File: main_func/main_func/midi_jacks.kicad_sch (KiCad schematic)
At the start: 13 parts, among them J4 MIDI_IN, J5 MIDI_THRU, J6 MIDI_OUT, J7 AudioJack4_Ground_SwitchTR1, J8 Conn_01x02_Male, U5 6N137

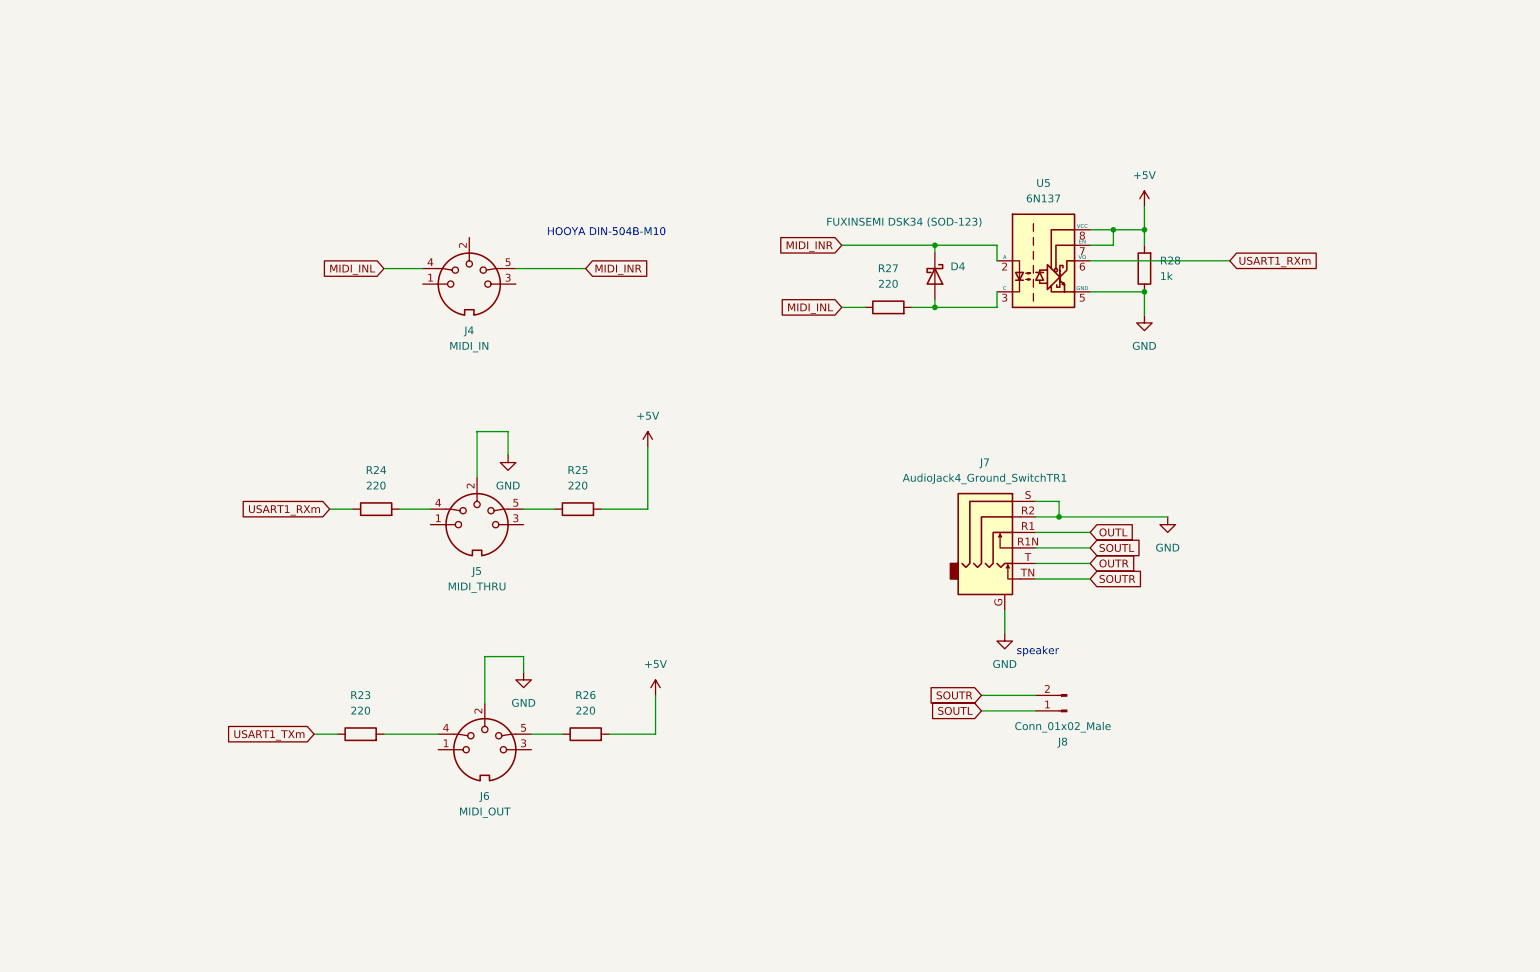
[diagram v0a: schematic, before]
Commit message: main func schematics fixed
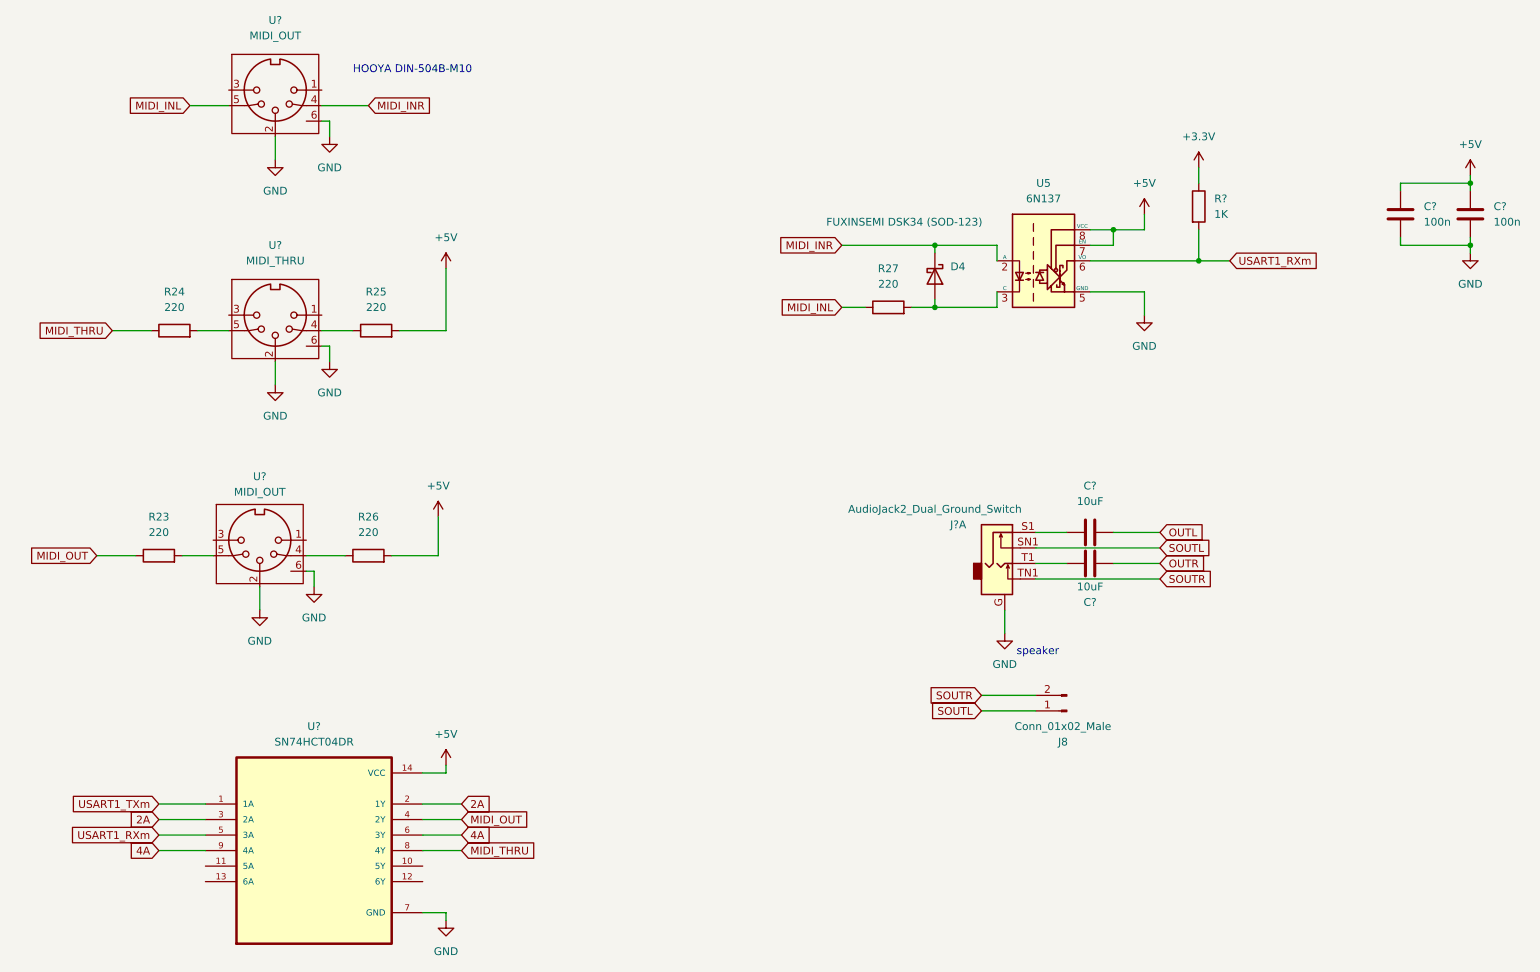
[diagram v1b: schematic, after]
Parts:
- removed J4: MIDI_IN, symbol Connector:DIN-5_180degree
- removed J5: MIDI_THRU, symbol Connector:DIN-5_180degree
- removed J6: MIDI_OUT, symbol Connector:DIN-5_180degree
- removed J7: AudioJack4_Ground_SwitchTR1, symbol Connector:AudioJack4_Ground_SwitchTR1
- removed R28: 1k, Resistor_SMD:R_0805_2012Metric_Pad1.20x1.40mm_HandSolder, symbol Device:R
- added C? (x2): 100n, Capacitor_SMD:C_0805_2012Metric_Pad1.18x1.45mm_HandSolder, symbol Device:C
- added C? (x2): 10uF, Capacitor_SMD:C_0805_2012Metric_Pad1.18x1.45mm_HandSolder, symbol Device:C
- added J?: AudioJack2_Dual_Ground_Switch, symbol Connector:AudioJack2_Dual_Ground_Switch
- added R?: 1K, Resistor_SMD:R_0805_2012Metric_Pad1.20x1.40mm_HandSolder, symbol Device:R
- added U? (x2): MIDI_OUT, midi:midi_7pin, symbol midi:midi5(+2)
- added U?: SN74HCT04DR, Package_SO:SOIC-14_3.9x8.7mm_P1.27mm, symbol SN74HCT04N:SN74HCT04N
- added U?: MIDI_THRU, midi:midi_7pin, symbol midi:midi5(+2)
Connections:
- net +5V: now also C?.1, C?.1, U?.14 (VCC)
- net GND: now also C?.2, C?.2, J?.G, U?.2, U?.2, U?.2, U?.6, U?.6, U?.6, U?.7 (GND)
- net MIDI_INL: now also U?.5
- net MIDI_INR: now also U?.4
- net OUTL: now also C?.2
- net OUTR: now also C?.2
- net SOUTL: now also J?.SN1
- net SOUTR: now also J?.TN1
- net USART1_RXm: now also R?.2, U?.5 (3A); no longer R24.1
- net USART1_TXm: now also U?.1 (1A); no longer R23.1
- net at R23.2: now also U?.5
- net at R24.2: now also U?.5
- net at R25.1: now also U?.4
- net at R26.1: now also U?.4
- new net: C?.1, J?.S1
- new net: C?.1, J?.T1
- new net +3V3: R?.1
- new net 2A: U?.2 (1Y), U?.3 (2A)
- new net 4A: U?.6 (3Y), U?.9 (4A)
- new net MIDI_OUT: R23.1, U?.4 (2Y)
- new net MIDI_THRU: R24.1, U?.8 (4Y)
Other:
- moved on the sheet: R23, R24, R25, R26

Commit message: fixing keyboard and pot project schematics
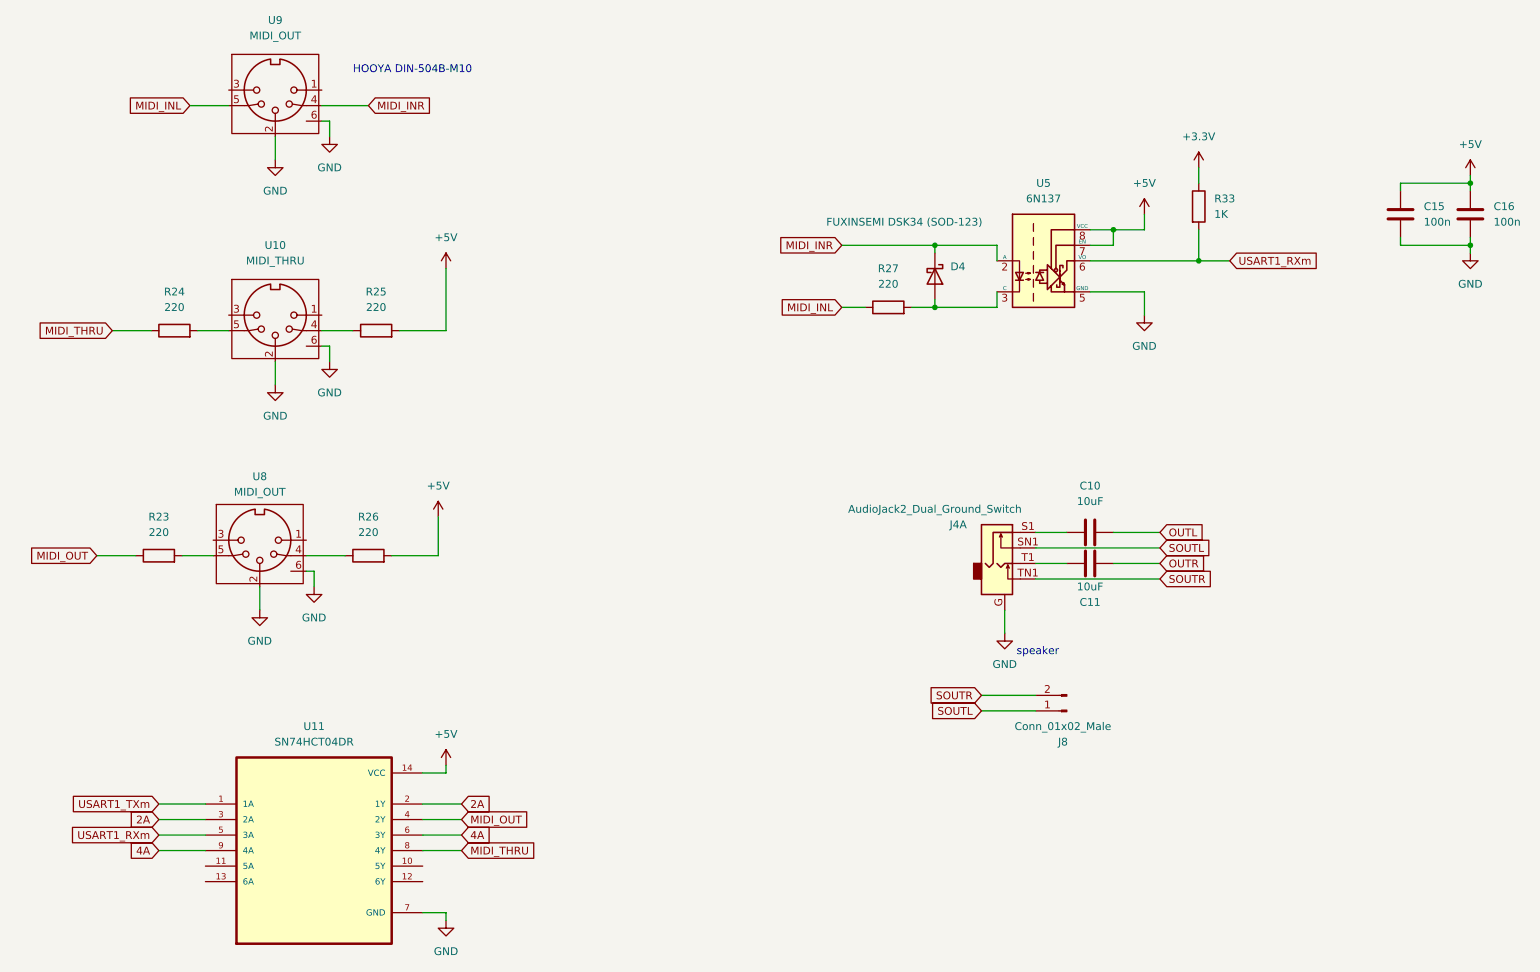
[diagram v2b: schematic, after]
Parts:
- gave numbers to parts that had none: 10
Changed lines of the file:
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@@
   (symbol (lib_id "midi:midi5(+2)") (at 63.5 32.766 0) (unit 1)
     (in_bom yes) (on_board yes) (fields_autoplaced)
-    (property "Reference" "U?" (id 0) (at 63.5 13.97 0))
+    (property "Reference" "U9" (id 0) (at 63.5 13.97 0))
     (property "Value" "MIDI_OUT" (id 1) (at 63.5 16.51 0))
     (property "Footprint" "midi:midi_7pin" (id 2) (at 86.868 23.876 0)
@@
   (symbol (lib_id "SN74HCT04N:SN74HCT04N") (at 69.85 149.86 0) (unit 1)
     (in_bom yes) (on_board yes) (fields_autoplaced)
-    (property "Reference" "U?" (id 0) (at 69.85 129.54 0))
+    (property "Reference" "U11" (id 0) (at 69.85 129.54 0))
     (property "Value" "SN74HCT04DR" (id 1) (at 69.85 132.08 0))
     (property "Footprint" "Package_SO:SOIC-14_3.9x8.7mm_P1.27mm" (id 2) (at 69.85 149.86 0)
@@
   (symbol (lib_id "power:GND") (at 63.5 36.83 0) (unit 1)
     (in_bom yes) (on_board yes) (fields_autoplaced)
-    (property "Reference" "#PWR?" (id 0) (at 63.5 43.18 0)
+    (property "Reference" "#PWR013" (id 0) (at 63.5 43.18 0)
       (effects (font (size 1.27 1.27)) hide)
     )
@@
   (symbol (lib_id "power:GND") (at 72.39 33.02 0) (unit 1)
     (in_bom yes) (on_board yes) (fields_autoplaced)
-    (property "Reference" "#PWR?" (id 0) (at 72.39 39.37 0)
+    (property "Reference" "#PWR015" (id 0) (at 72.39 39.37 0)
       (effects (font (size 1.27 1.27)) hide)
     )
@@
   (symbol (lib_id "power:+5V") (at 259.08 39.37 0) (unit 1)
     (in_bom yes) (on_board yes) (fields_autoplaced)
-    (property "Reference" "#PWR?" (id 0) (at 259.08 43.18 0)
+    (property "Reference" "#PWR023" (id 0) (at 259.08 43.18 0)
       (effects (font (size 1.27 1.27)) hide)
     )
@@
   (symbol (lib_id "power:GND") (at 91.44 161.29 0) (unit 1)
     (in_bom yes) (on_board yes) (fields_autoplaced)
-    (property "Reference" "#PWR?" (id 0) (at 91.44 167.64 0)
+    (property "Reference" "#PWR020" (id 0) (at 91.44 167.64 0)
       (effects (font (size 1.27 1.27)) hide)
     )
@@
   (symbol (lib_id "Connector:AudioJack2_Dual_Ground_Switch") (at 182.88 102.87 0) (unit 1)
     (in_bom yes) (on_board yes)
-    (property "Reference" "J?" (id 0) (at 175.26 96.52 0))
+    (property "Reference" "J4" (id 0) (at 175.26 96.52 0))
     (property "Value" "AudioJack2_Dual_Ground_Switch" (id 1) (at 171.45 93.98 0))
     (property "Footprint" "" (id 2) (at 181.61 97.79 0)
@@
   (symbol (lib_id "power:GND") (at 259.08 52.07 0) (unit 1)
     (in_bom yes) (on_board yes) (fields_autoplaced)
-    (property "Reference" "#PWR?" (id 0) (at 259.08 58.42 0)
+    (property "Reference" "#PWR025" (id 0) (at 259.08 58.42 0)
       (effects (font (size 1.27 1.27)) hide)
     )
@@
   (symbol (lib_id "Device:R") (at 214.63 44.45 0) (unit 1)
     (in_bom yes) (on_board yes) (fields_autoplaced)
-    (property "Reference" "R?" (id 0) (at 217.17 43.1799 0)
+    (property "Reference" "R33" (id 0) (at 217.17 43.1799 0)
       (effects (font (size 1.27 1.27)) (justify left))
     )
@@
   (symbol (lib_id "power:GND") (at 69.85 106.68 0) (unit 1)
     (in_bom yes) (on_board yes) (fields_autoplaced)
-    (property "Reference" "#PWR?" (id 0) (at 69.85 113.03 0)
+    (property "Reference" "#PWR014" (id 0) (at 69.85 113.03 0)
       (effects (font (size 1.27 1.27)) hide)
     )
@@
   (symbol (lib_id "midi:midi5(+2)") (at 63.5 69.596 0) (unit 1)
     (in_bom yes) (on_board yes) (fields_autoplaced)
-    (property "Reference" "U?" (id 0) (at 63.5 50.8 0))
+    (property "Reference" "U10" (id 0) (at 63.5 50.8 0))
     (property "Value" "MIDI_THRU" (id 1) (at 63.5 53.34 0))
     (property "Footprint" "midi:midi_7pin" (id 2) (at 86.868 60.706 0)
@@
   (symbol (lib_id "power:+3.3V") (at 214.63 38.1 0) (unit 1)
     (in_bom yes) (on_board yes) (fields_autoplaced)
-    (property "Reference" "#PWR?" (id 0) (at 214.63 41.91 0)
+    (property "Reference" "#PWR021" (id 0) (at 214.63 41.91 0)
       (effects (font (size 1.27 1.27)) hide)
     )
@@
   (symbol (lib_id "Device:C") (at 247.65 45.72 0) (unit 1)
     (in_bom yes) (on_board yes) (fields_autoplaced)
-    (property "Reference" "C?" (id 0) (at 251.46 44.4499 0)
+    (property "Reference" "C15" (id 0) (at 251.46 44.4499 0)
       (effects (font (size 1.27 1.27)) (justify left))
     )
@@
   (symbol (lib_id "Device:C") (at 196.85 97.79 90) (unit 1)
     (in_bom yes) (on_board yes) (fields_autoplaced)
-    (property "Reference" "C?" (id 0) (at 196.85 90.17 90))
+    (property "Reference" "C10" (id 0) (at 196.85 90.17 90))
     (property "Value" "10uF" (id 1) (at 196.85 92.71 90))
     (property "Footprint" "Capacitor_SMD:C_0805_2012Metric_Pad1.18x1.45mm_HandSolder" (id 2) (at 200.66 96.8248 0)
@@
   (symbol (lib_id "power:GND") (at 72.39 69.85 0) (unit 1)
     (in_bom yes) (on_board yes) (fields_autoplaced)
-    (property "Reference" "#PWR?" (id 0) (at 72.39 76.2 0)
+    (property "Reference" "#PWR018" (id 0) (at 72.39 76.2 0)
       (effects (font (size 1.27 1.27)) hide)
     )
@@
   (symbol (lib_id "power:+5V") (at 91.44 135.89 0) (unit 1)
     (in_bom yes) (on_board yes) (fields_autoplaced)
-    (property "Reference" "#PWR?" (id 0) (at 91.44 139.7 0)
+    (property "Reference" "#PWR019" (id 0) (at 91.44 139.7 0)
       (effects (font (size 1.27 1.27)) hide)
     )
@@
   (symbol (lib_id "Device:C") (at 196.85 102.87 90) (unit 1)
     (in_bom yes) (on_board yes)
-    (property "Reference" "C?" (id 0) (at 196.85 109.22 90))
+    (property "Reference" "C11" (id 0) (at 196.85 109.22 90))
     (property "Value" "10uF" (id 1) (at 196.85 106.68 90))
     (property "Footprint" "Capacitor_SMD:C_0805_2012Metric_Pad1.18x1.45mm_HandSolder" (id 2) (at 200.66 101.9048 0)
@@
   (symbol (lib_id "Device:C") (at 259.08 45.72 0) (unit 1)
     (in_bom yes) (on_board yes) (fields_autoplaced)
-    (property "Reference" "C?" (id 0) (at 262.89 44.4499 0)
+    (property "Reference" "C16" (id 0) (at 262.89 44.4499 0)
       (effects (font (size 1.27 1.27)) (justify left))
     )
@@
   (symbol (lib_id "midi:midi5(+2)") (at 60.96 106.426 0) (unit 1)
     (in_bom yes) (on_board yes) (fields_autoplaced)
-    (property "Reference" "U?" (id 0) (at 60.96 88.646 0))
+    (property "Reference" "U8" (id 0) (at 60.96 88.646 0))
     (property "Value" "MIDI_OUT" (id 1) (at 60.96 91.186 0))
     (property "Footprint" "midi:midi_7pin" (id 2) (at 84.328 97.536 0)

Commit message: main_func pcb done
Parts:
- C10, C11: value 10uF -> 10u; footprint Capacitor_SMD:C_0805_2012Metric_Pad1.18x1.45mm_HandSolder -> Capacitor_THT:C_Rect_L33.0mm_W15.0mm_P27.50mm_MKS4
- J4: value AudioJack2_Dual_Ground_Switch -> Korean Hroparts Elec PJ-3250-5A; footprint (none) -> Korean Hroparts Elec PJ-3250-5A:Korean Hroparts Elec PJ-3250-5A
- J8: footprint (none) -> Connector_PinSocket_2.54mm:PinSocket_1x02_P2.54mm_Horizontal
- U9: value MIDI_OUT -> MIDI_IN
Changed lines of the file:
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@@
   (global_label "USART1_RXm" (shape input) (at 44.45 147.32 180) (fields_autoplaced)
     (effects (font (size 1.27 1.27)) (justify right))
-    (property "Intersheet References" "${INTERSHEET_REFS}" (id 0) (at 29.8207 147.3994 0)
+    (property "Intersheet References" "${INTERSHEET_REFS}" (id 0) (at 29.8207 147.2406 0)
       (effects (font (size 1.27 1.27)) (justify right) hide)
     )
@@
   (global_label "USART1_TXm" (shape input) (at 44.45 142.24 180) (fields_autoplaced)
     (effects (font (size 1.27 1.27)) (justify right))
-    (property "Intersheet References" "${INTERSHEET_REFS}" (id 0) (at 30.1231 142.3194 0)
+    (property "Intersheet References" "${INTERSHEET_REFS}" (id 0) (at 30.1231 142.1606 0)
       (effects (font (size 1.27 1.27)) (justify right) hide)
     )
@@
     (in_bom yes) (on_board yes) (fields_autoplaced)
     (property "Reference" "U9" (id 0) (at 63.5 13.97 0))
-    (property "Value" "MIDI_OUT" (id 1) (at 63.5 16.51 0))
+    (property "Value" "MIDI_IN" (id 1) (at 63.5 16.51 0))
     (property "Footprint" "midi:midi_7pin" (id 2) (at 86.868 23.876 0)
       (effects (font (size 1.27 1.27)) hide)
@@
     (property "Reference" "J8" (id 0) (at 192.405 132.08 0))
     (property "Value" "Conn_01x02_Male" (id 1) (at 192.405 129.54 0))
-    (property "Footprint" "" (id 2) (at 193.04 127 0)
+    (property "Footprint" "Connector_PinSocket_2.54mm:PinSocket_1x02_P2.54mm_Horizontal" (id 2) (at 193.04 127 0)
       (effects (font (size 1.27 1.27)) hide)
     )
@@
     (in_bom yes) (on_board yes)
     (property "Reference" "J4" (id 0) (at 175.26 96.52 0))
-    (property "Value" "AudioJack2_Dual_Ground_Switch" (id 1) (at 171.45 93.98 0))
-    (property "Footprint" "" (id 2) (at 181.61 97.79 0)
+    (property "Value" "Korean Hroparts Elec PJ-3250-5A" (id 1) (at 171.45 93.98 0))
+    (property "Footprint" "Korean Hroparts Elec PJ-3250-5A:Korean Hroparts Elec PJ-3250-5A" (id 2) (at 181.61 97.79 0)
       (effects (font (size 1.27 1.27)) hide)
     )
@@
     (in_bom yes) (on_board yes) (fields_autoplaced)
     (property "Reference" "C10" (id 0) (at 196.85 90.17 90))
-    (property "Value" "10uF" (id 1) (at 196.85 92.71 90))
-    (property "Footprint" "Capacitor_SMD:C_0805_2012Metric_Pad1.18x1.45mm_HandSolder" (id 2) (at 200.66 96.8248 0)
+    (property "Value" "10u" (id 1) (at 196.85 92.71 90))
+    (property "Footprint" "Capacitor_THT:C_Rect_L33.0mm_W15.0mm_P27.50mm_MKS4" (id 2) (at 200.66 96.8248 0)
       (effects (font (size 1.27 1.27)) hide)
     )
@@
     (in_bom yes) (on_board yes)
     (property "Reference" "C11" (id 0) (at 196.85 109.22 90))
-    (property "Value" "10uF" (id 1) (at 196.85 106.68 90))
-    (property "Footprint" "Capacitor_SMD:C_0805_2012Metric_Pad1.18x1.45mm_HandSolder" (id 2) (at 200.66 101.9048 0)
-      (effects (font (size 1.27 1.27)) hide)
-    )
+    (property "Value" "10u" (id 1) (at 196.85 106.68 90))
+    (property "Footprint" "Capacitor_THT:C_Rect_L33.0mm_W15.0mm_P27.50mm_MKS4" (id 2) (at 200.66 101.9048 0)
+      (effects (font (size 1.27 1.27)) hide)
+    )

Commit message: Pot.but_pcb in progress
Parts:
- J8: footprint Connector_PinSocket_2.54mm:PinSocket_1x02_P2.54mm_Horizontal -> Capacitor_THT:C_Rect_L7.5mm_W6.5mm_P5.00mm
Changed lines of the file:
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@@
     (property "Reference" "J8" (id 0) (at 192.405 132.08 0))
     (property "Value" "Conn_01x02_Male" (id 1) (at 192.405 129.54 0))
-    (property "Footprint" "Connector_PinSocket_2.54mm:PinSocket_1x02_P2.54mm_Horizontal" (id 2) (at 193.04 127 0)
+    (property "Footprint" "Capacitor_THT:C_Rect_L7.5mm_W6.5mm_P5.00mm" (id 2) (at 193.04 127 0)
       (effects (font (size 1.27 1.27)) hide)
     )
